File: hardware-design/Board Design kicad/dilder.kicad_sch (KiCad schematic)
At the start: 35 parts, among them J1 USB-C, J2 JST-PH-2, J3 ePaper 8pin, Q1 FS8205A, SW1 5-Way Nav, U1 RP2040, U2 TP4056, U3 DW01A, U4 AMS1117-3.3, U5 W25Q16JV, U6 MPU-6050, U7 ATGM336H, Y1 12MHz

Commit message: Replace RP2040 with ESP32-S3-WROOM-1-N16R8 in schematic, add BOM, Prompt #149
Rewrote generate_schematic.py: removed RP2040, W25Q16JV flash, 12MHz crystal,
27R USB resistors, and ATGM336H GPS. Added ESP32-S3 module with all nets wired
(SPI e-paper, I2C IMU, USB-OTG direct, joystick GPIO4-8, EN pull-up).
Component count 33→20. Added BOM.md and updated Measurements.md.

Co-Authored-By: Claude Opus 4.6 (1M context) <noreply@anthropic.com>
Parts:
- removed C1, C2: 15pF, Capacitor_SMD:C_0402_1005Metric, symbol C
- removed C8: 100nF, Capacitor_SMD:C_0402_1005Metric, symbol C
- removed R6, R7: 27R, Resistor_SMD:R_0402_1005Metric, symbol R
- removed U5: W25Q16JV, Package_SO:SOIC-8_3.9x4.9mm_P1.27mm, symbol W25Q16JV
- removed U7: ATGM336H, symbol ATGM336H
- removed Y1: 12MHz, Crystal:Crystal_SMD_3215-2Pin_3.2x1.5mm, symbol Crystal_12MHz
- J3: footprint Connector_PinHeader_2.54mm:PinHeader_1x08_P2.54mm_Vertical -> Connector_JST:JST_SH_SM08B-SRSS-TB_1x08-1MP_P1.00mm_Horizontal
- U1: value RP2040 -> ESP32-S3-N16R8; footprint Package_DFN_QFN:QFN-56-1EP_7x7mm_P0.4mm_EP3.2x3.2mm -> RF_Module:ESP32-S3-WROOM-1; symbol RP2040 -> ESP32-S3-WROOM-1; LCSC C2040 -> C2913196
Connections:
- net GPIO0 is gone; now on net 3V3: U1.2 (3V3)
- net USB_DM_IN is gone; now on net USB_DM: J1.A7 (D-)
- net USB_DP_IN is gone; now on net USB_DP: J1.A6 (D+)
- net XIN is gone; now on net EPD_BUSY: U1.20 (GPIO12/BUSY)
- net XOUT is gone; now on net EPD_CS: U1.19 (GPIO46/CS)
- net 3V3: no longer U1.1 (IOVDD), U1.26 (QSPI_SS), U1.43 (ADC_AVDD), U1.44 (VREG_VIN), U1.48 (DVDD), U1.50 (USB_VDD)
- net CC2: now also U1.1 (GND); no longer U1.49 (TESTEN), U1.57 (GND)
- net USB_DM: now also U1.13 (GPIO19/D-); no longer U1.46 (USB_DM)
- net USB_DP: now also U1.14 (GPIO20/D+); no longer U1.47 (USB_DP)
- net I2C_SDA: now reaches U1.9 (GPIO16/SDA)
- net I2C_SDA: now also R4.2, U6.24 (SDA)
- net GPIO1 renamed EN
- net EN: now also R10.2
- net GPIO10 renamed EPD_CLK
- net EPD_CLK: now also U1.15 (GPIO9/SCK); no longer U1.12 (GPIO10)
- net GPIO11 renamed EPD_MOSI
- net EPD_MOSI: now also U1.16 (GPIO10/MOSI); no longer U1.13 (GPIO11)
- net GPIO12 renamed EPD_RST
- net EPD_RST: now also U1.18 (GPIO11/RST); no longer U1.14 (GPIO12)
- net GPIO13 renamed EPD_BUSY
- net EPD_BUSY: no longer U1.15 (GPIO13)
- removed net GPIO14: R4.2, U1.16 (GPIO14), U6.24 (SDA)
- net GPIO15 renamed I2C_SCL
- net I2C_SCL: now also U1.10 (GPIO17/SCL); no longer U1.17 (GPIO15)
- net GPIO2 renamed JOY_UP
- net GPIO3 renamed JOY_DOWN
- net GPIO4 renamed JOY_LEFT
- net GPIO5 renamed JOY_RIGHT
- net GPIO6 renamed JOY_CENTER
- net GPIO8 renamed EPD_DC
- net EPD_DC: now also U1.17 (GPIO3/DC); no longer U1.10 (GPIO8)
- net GPIO9 renamed EPD_CS
- net EPD_CS: no longer U1.11 (GPIO9)
- removed net QSPI_SCLK: U1.24 (QSPI_SCLK)
- removed net QSPI_SD0: U1.21 (QSPI_SD0)
- removed net QSPI_SD1: U1.22 (QSPI_SD1)
- removed net RUN: R10.2, U1.18 (RUN)
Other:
- note added: "GPIO16/17=I2C(SDA/SCL) GPIO19/20=USB(D-/D+) Native USB-OTG, no series resistors"
- note added: "GPIO4-8=Joystick GPIO9/10=SPI(CLK/MOSI) GPIO3=DC GPIO11=RST GPIO46=CS GPIO12=BUSY"
- note added: "MCU: ESP32-S3-WROOM-1-N16R8 (WiFi+BLE, 16MB flash, 8MB PSRAM)"
- note removed: "GPIO0=GPS_RX GPIO1=GPS_TX GPIO2-6=Joystick GPIO8-13=ePaper SPI1 GPIO14/15=IMU I2C0"
- note removed: "MCU: RP2040 (C2040) + W25Q16JV Flash + 12MHz Crystal"

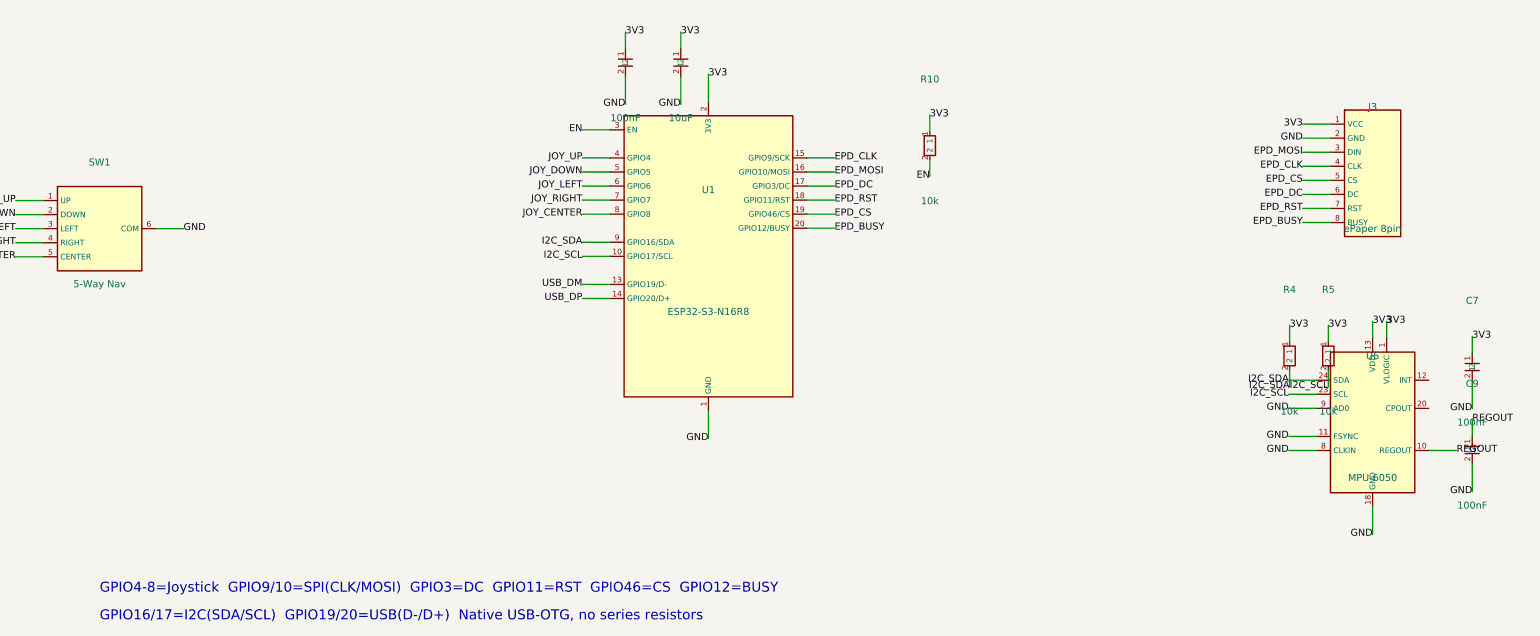
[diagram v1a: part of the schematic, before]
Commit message: Add v0.4 PCB routing, board design doc, update prompts, Prompt #155
Route the v0.4 board (30x70mm, 4-layer) with route_v04.py: B.Cu channels
for I2C/USB/joystick/ePaper, staggered L-routes for crossing-free SPI,
custom paths for EN/BOOT/battery protection, F.Cu power chain. Adds In1.Cu
GND plane and In2.Cu 3V3 plane with stitching vias. Board design doc
captures zones, BOM, GPIO map, routing strategy, and DRC status. Updates
prompts index with #154-155.

Co-Authored-By: Claude Opus 4.6 (1M context) <noreply@anthropic.com>
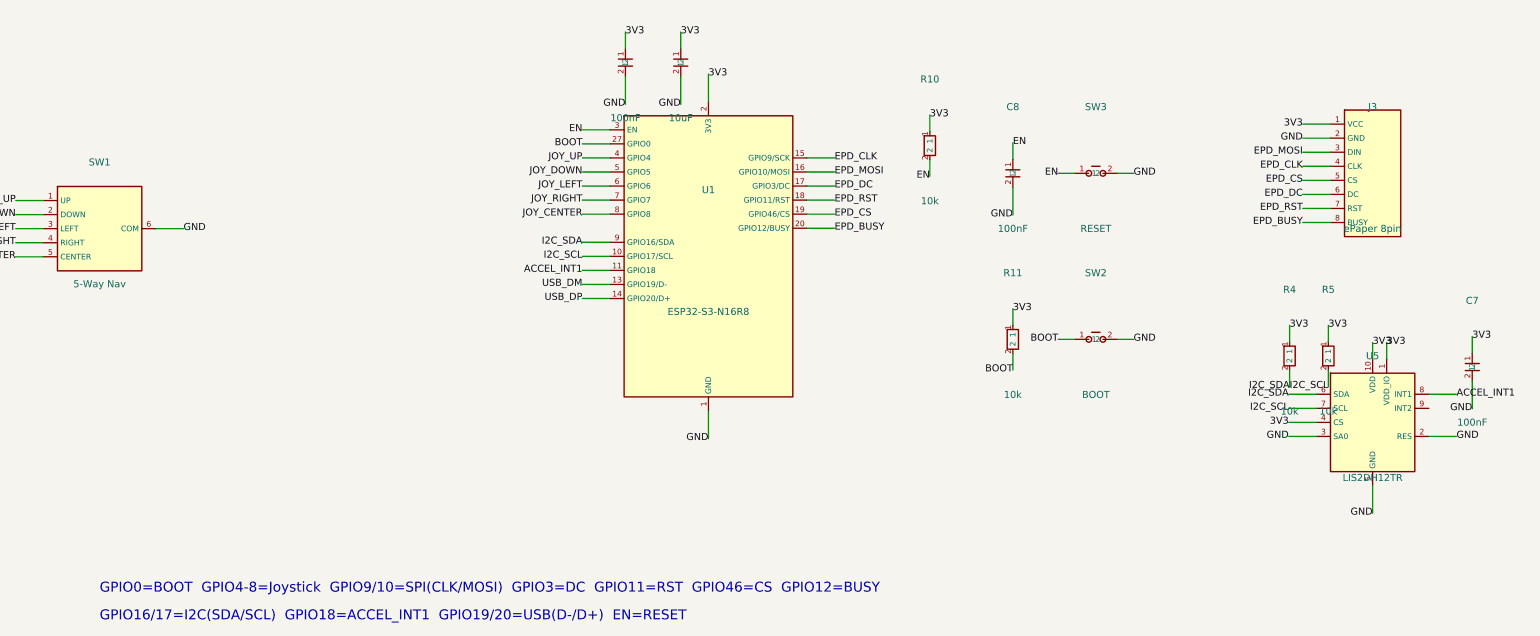
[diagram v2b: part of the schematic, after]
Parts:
- removed C9: 100nF, Capacitor_SMD:C_0402_1005Metric, symbol C
- removed U6: MPU-6050, Package_DFN_QFN:QFN-24-1EP_4x4mm_P0.5mm_EP2.7x2.7mm, symbol MPU-6050
- added C8: 100nF, Capacitor_SMD:C_0402_1005Metric, symbol C
- added R11: 10k, Resistor_SMD:R_0402_1005Metric, symbol R
- added SW2: BOOT, Button_Switch_SMD:SW_SPST_PTS810, symbol SW_Push
- added SW3: RESET, Button_Switch_SMD:SW_SPST_PTS810, symbol SW_Push
- added U5: LIS2DH12TR, Package_LGA:LGA-12_2x2mm_P0.5mm, symbol LIS2DH12TR
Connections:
- net 3V3: now also R11.1, U5.1 (VDD_IO), U5.10 (VDD), U5.4 (CS)
- net CC2: now also C8.2, SW2.2, SW3.2, U5.2 (RES), U5.3 (SA0), U5.5 (GND)
- net EN: now also C8.1, SW3.1
- net I2C_SCL: now also U5.7 (SCL)
- net I2C_SDA: now also U5.6 (SDA)
- new net ACCEL_INT1: U1.11 (GPIO18), U5.8 (INT1)
- new net BOOT: R11.2, SW2.1, U1.27 (GPIO0)
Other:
- note added: "GPIO0=BOOT GPIO4-8=Joystick GPIO9/10=SPI(CLK/MOSI) GPIO3=DC GPIO11=RST GPIO46=CS GPIO12=BUSY"
- note added: "GPIO16/17=I2C(SDA/SCL) GPIO18=ACCEL_INT1 GPIO19/20=USB(D-/D+) EN=RESET"
- note removed: "GPIO16/17=I2C(SDA/SCL) GPIO19/20=USB(D-/D+) Native USB-OTG, no series resistors"
- note removed: "GPIO4-8=Joystick GPIO9/10=SPI(CLK/MOSI) GPIO3=DC GPIO11=RST GPIO46=CS GPIO12=BUSY"

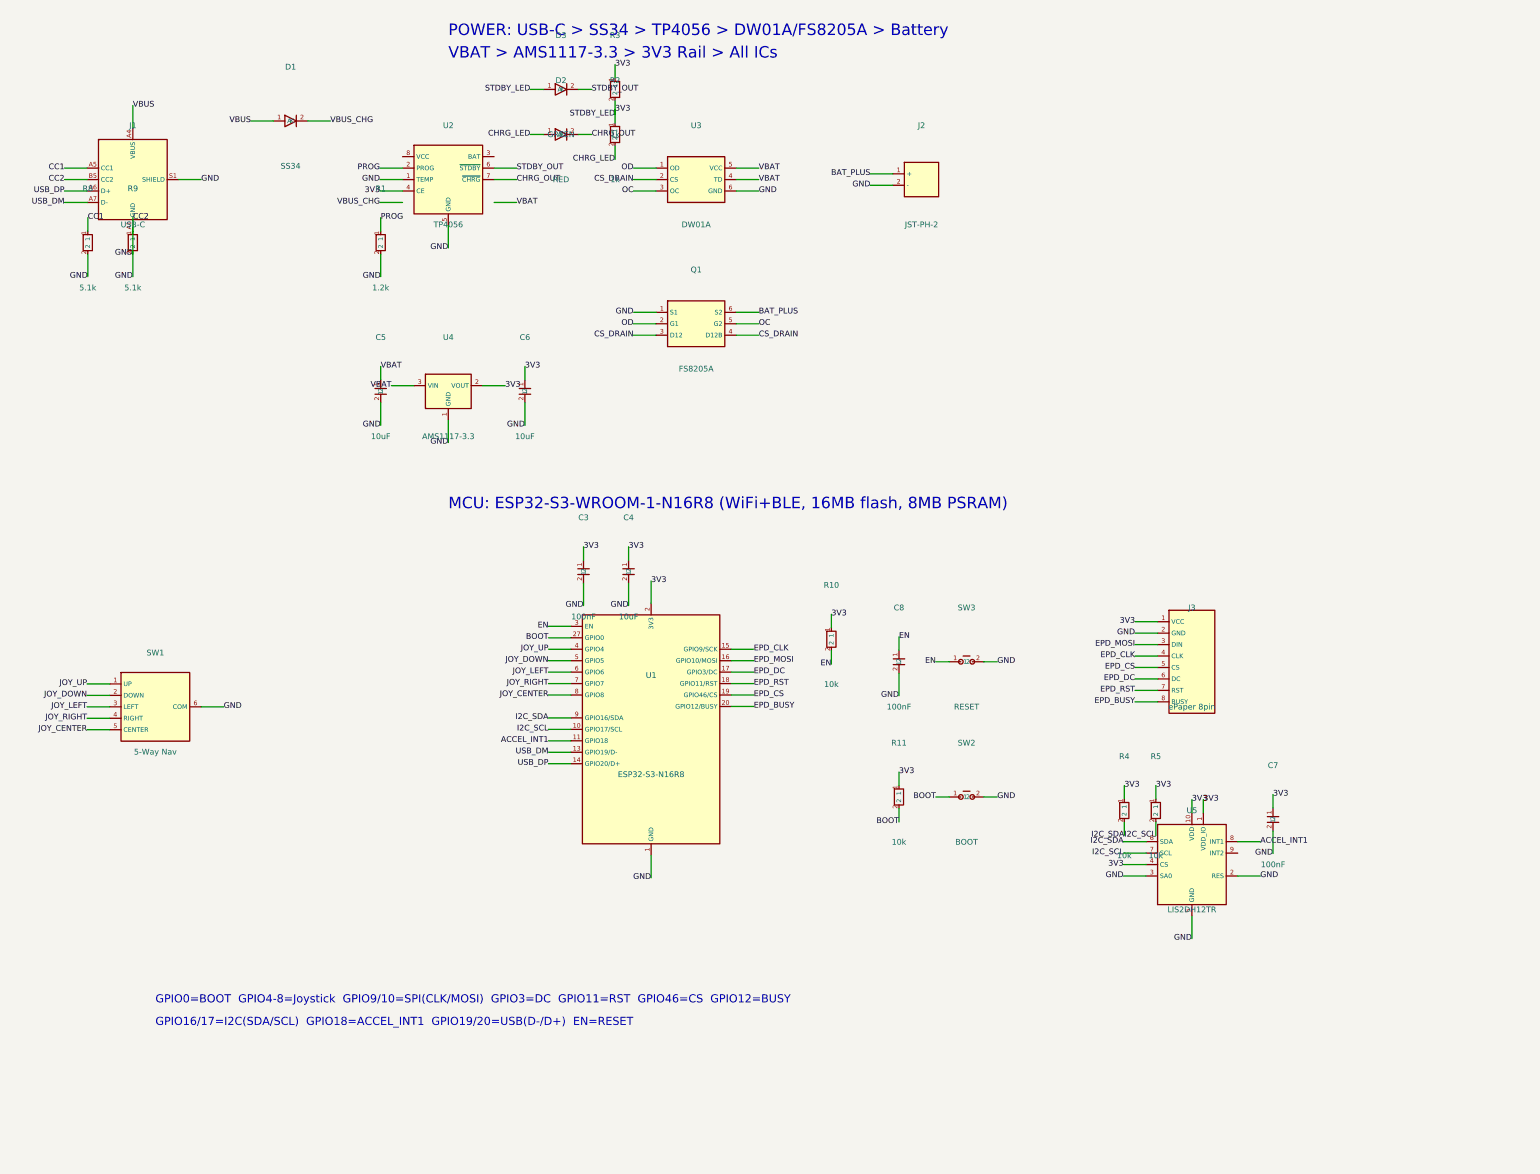
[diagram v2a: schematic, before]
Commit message: Add user guide, asset system, feature menus, KiCad sensor updates, blog posts, Prompt #162
User guide (1,207 lines) covering all planned features as if implemented:
story, 16 emotions, stat system, 64 achievements, 6 evolutions, controls.
Feature systems doc (963 lines) with achievement registry, menu viewer
specs, toast notifications, decor browser, and full menu hierarchy.

Asset rendering pipeline: 52 Python modules generating 22 environments,
42 outfits, 29 decor props, 16 aura particle sets, and emotion previews.
Grid compilation images copied to website for blog showcases.

KiCad schematic + PCB updated with AHT20 and BH1750 sensors on shared
I2C bus. BOM, board design docs, wiring pinout updated accordingly.

New blog post on asset rendering system with image showcases.
User guide published to website docs. Prompts #161-#162 logged.

Co-Authored-By: Claude Opus 4.6 (1M context) <noreply@anthropic.com>
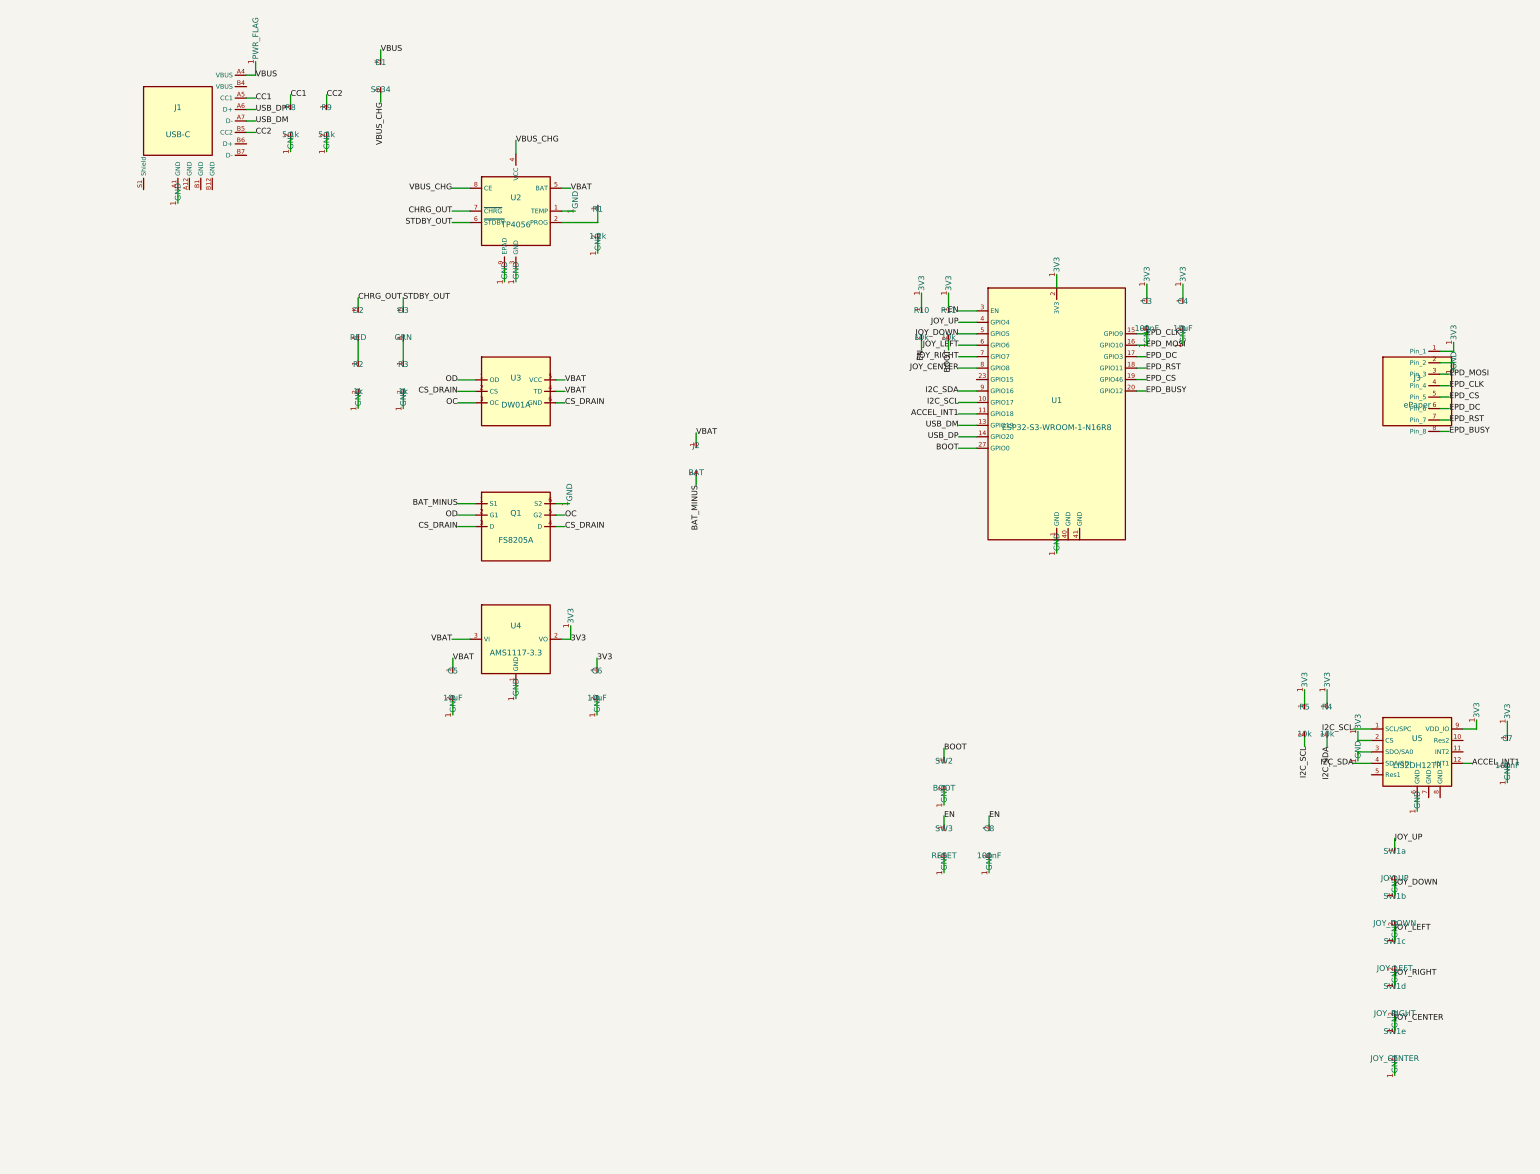
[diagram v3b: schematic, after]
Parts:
- removed J1: USB-C, symbol USB_C_16P
- removed J3: ePaper 8pin, Connector_JST:JST_SH_SM08B-SRSS-TB_1x08-1MP_P1.00mm_Horizontal, symbol EPAPER_HEADER
- removed SW1: 5-Way Nav, symbol SKRHABE010
- removed U1: ESP32-S3-N16R8, RF_Module:ESP32-S3-WROOM-1, symbol ESP32-S3-WROOM-1
- removed U4: AMS1117-3.3, Package_TO_SOT_SMD:SOT-223-3_TabPin2, symbol AMS1117-3.3
- added J1: USB-C, Connector_USB:USB_C_Receptacle_HRO_TYPE-C-31-M-12, symbol USB_C
- added J3: ePaper, Connector_JST:JST_SH_SM08B-SRSS-TB_1x08-1MP_P1.00mm_Horizontal, symbol EPAPER_HDR
- added SW1a: JOY_UP, symbol SW_Push
- added SW1b: JOY_DOWN, symbol SW_Push
- added SW1c: JOY_LEFT, symbol SW_Push
- added SW1d: JOY_RIGHT, symbol SW_Push
- added SW1e: JOY_CENTER, symbol SW_Push
- added U1: ESP32-S3-WROOM-1-N16R8, RF_Module:ESP32-S3-WROOM-1, symbol ESP32_S3_WROOM_1
- added U4: AMS1117-3.3, Package_TO_SOT_SMD:SOT-223-3_TabPin2, symbol AMS1117_3V3
- D3: value GREEN -> GRN
- J2: value JST-PH-2 -> BAT; footprint Connector_JST:JST_PH_S2B-PH-SM4-TB_1x02-1MP_P2.00mm_Horizontal -> Connector_JST:JST_PH_B2B-PH-SM4-TB_1x02-1MP_P2.00mm_Vertical
- SW2, SW3: footprint Button_Switch_SMD:SW_SPST_PTS810 -> (none)
- U2: footprint Package_SO:ESOP-8_3.9x4.9mm_P1.27mm -> Package_SO:SOIC-8-1EP_3.9x4.9mm_P1.27mm_EP2.41x3.3mm_ThermalVias
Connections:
- net 3V3: now also U5.2 (CS), U5.9 (VDD_IO), J3.1 (Pin_1), U1.2 (3V3), U4.2 (VO); no longer D3.1 (A), R2.1, R3.1, R3.2, U2.4 (CE), U5.1 (VDD_IO), U5.10 (VDD), U5.4 (CS)
- net ACCEL_INT1: now also U5.12 (INT1), U1.11 (GPIO18); no longer U5.8 (INT1)
- net BOOT: now also U1.27 (GPIO0)
- net CC1: now also J1.A5 (CC1)
- net CC2: now also J1.B5 (CC2); no longer C3.2, C4.2, C5.2, C6.2, C7.2, C8.2, J2.2 (-), Q1.1 (S1), R1.2, R8.2, R9.2, SW2.2, SW3.2, U2.1 (TEMP), U2.5 (GND), U3.6 (GND), U5.2 (RES), U5.3 (SA0), U5.5 (GND)
- net CHRG_OUT: now also D2.K; no longer D2.2 (K)
- net CS_DRAIN: now also U3.6 (GND)
- net EN: now also U1.3 (EN)
- net EPD_BUSY: now also J3.8 (Pin_8), U1.20 (GPIO12)
- net EPD_CLK: now also J3.4 (Pin_4), U1.15 (GPIO9)
- net EPD_CS: now also J3.5 (Pin_5), U1.19 (GPIO46)
- net EPD_DC: now also J3.6 (Pin_6), U1.17 (GPIO3)
- net EPD_MOSI: now also J3.3 (Pin_3), U1.16 (GPIO10)
- net EPD_RST: now also J3.7 (Pin_7), U1.18 (GPIO11)
- net I2C_SCL: now also U5.1 (SCL/SPC), U1.10 (GPIO17); no longer U5.7 (SCL)
- net I2C_SDA: now also U5.4 (SDA/SDI), U1.9 (GPIO16); no longer U5.6 (SDA)
- net JOY_UP: now also SW1a.1, U1.4 (GPIO4)
- net STDBY_OUT: now also D3.K; no longer D3.2 (K)
- net USB_DM: now also J1.A7 (D-), U1.13 (GPIO19)
- net USB_DP: now also J1.A6 (D+), U1.14 (GPIO20)
- net VBAT: now also J2.1, U2.5 (BAT), U4.3 (VI)
- net VBUS_CHG: now also D1.A, U2.4 (VCC), U2.8 (CE); no longer D1.2 (K)
- net GND: now reaches U2.3 (GND)
- net GND: now also C3.2, C4.2, C5.2, C6.2, C7.2, C8.2, Q1.6 (S2), R1.2, R2.2, R3.2, R8.2, R9.2, SW2.2, SW3.2, U2.1 (TEMP), U2.9 (EPAD), U5.3 (SDO/SA0), U5.6 (GND), J1.A1 (GND), J3.2 (Pin_2), SW1a.2, SW1b.1, SW1b.2, SW1c.1, SW1c.2, SW1d.1, SW1d.2, SW1e.1, SW1e.2, U1.1 (GND), U1.5 (GPIO5), U1.6 (GPIO6), U1.7 (GPIO7), U1.8 (GPIO8), U4.1 (GND)
- removed net BAT_PLUS: J2.1 (+), Q1.6 (S2)
- removed net CHRG_LED: D2.1 (A), R2.2
- net PROG: no longer names the net of R1.1, U2.2 (PROG)
- removed net VBUS: D1.1 (A)
- new net: D2.A, R2.1
- new net: D3.A, R3.1
- new net BAT_MINUS: J2.2, Q1.1 (S1)
- new net PWR_FLAG: D1.K, J1.A4 (VBUS)
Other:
- note removed: "GPIO0=BOOT GPIO4-8=Joystick GPIO9/10=SPI(CLK/MOSI) GPIO3=DC GPIO11=RST GPIO46=CS GPIO12=BUSY"
- note removed: "GPIO16/17=I2C(SDA/SCL) GPIO18=ACCEL_INT1 GPIO19/20=USB(D-/D+) EN=RESET"
- note removed: "MCU: ESP32-S3-WROOM-1-N16R8 (WiFi+BLE, 16MB flash, 8MB PSRAM)"
- note removed: "POWER: USB-C > SS34 > TP4056 > DW01A/FS8205A > Battery"
- note removed: "VBAT > AMS1117-3.3 > 3V3 Rail > All ICs"
